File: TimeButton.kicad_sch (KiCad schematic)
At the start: 14 parts, among them P1 USB_C_Plug_USB2.0, U1 PIC18F15Q41-I/SS, U2 FT231XS

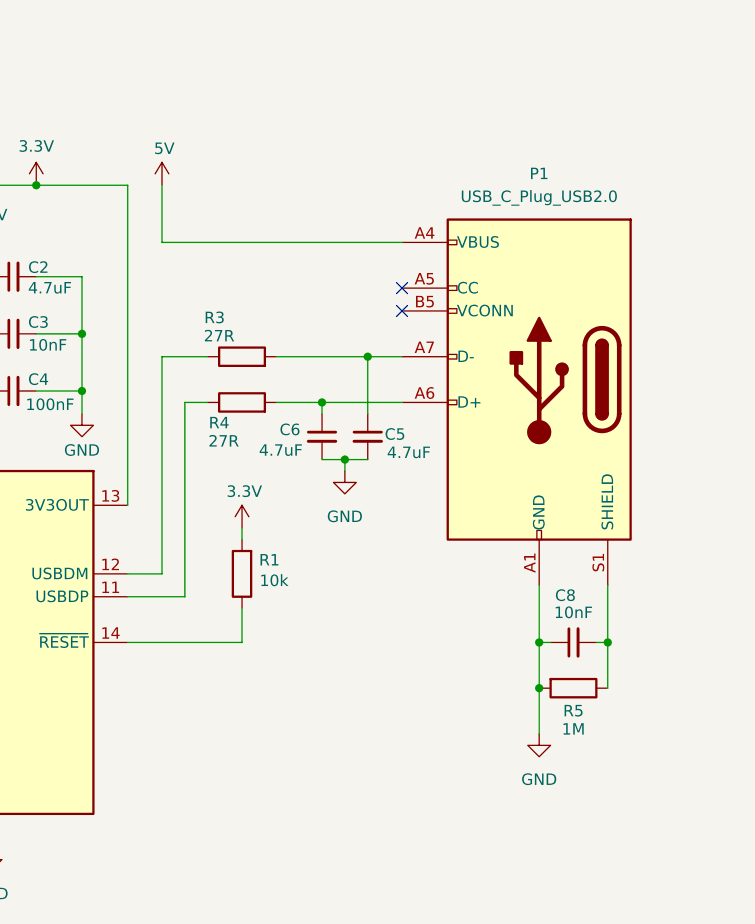
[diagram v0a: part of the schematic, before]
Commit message: Changed USB_C connector from 6Pin to 16Pin
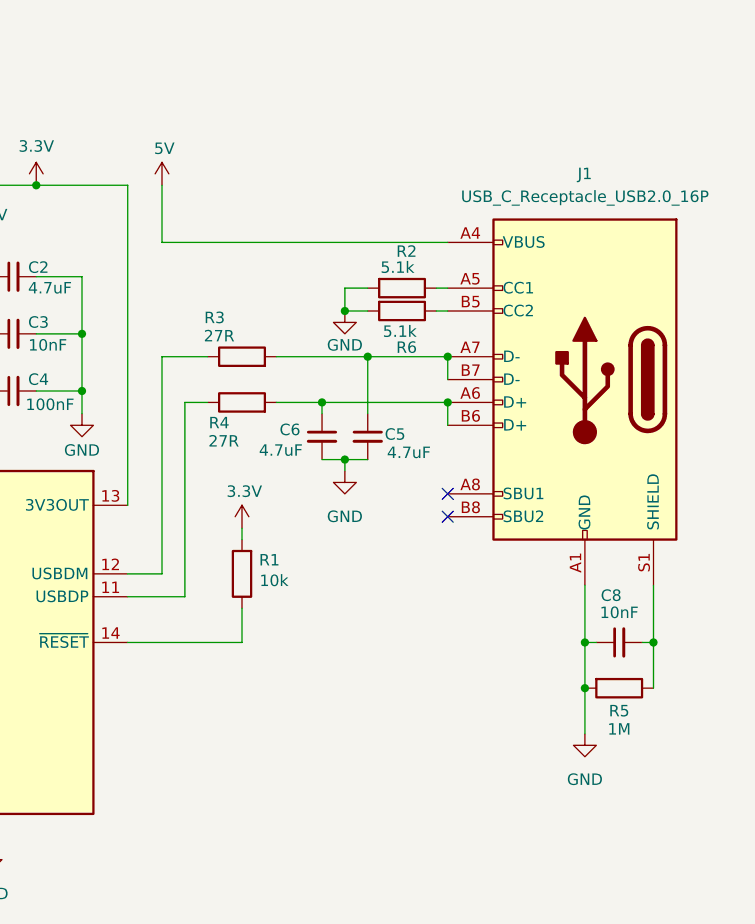
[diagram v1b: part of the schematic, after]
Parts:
- removed P1: USB_C_Plug_USB2.0, Connector_USB:USB_C_Receptacle_HRO_TYPE-C-31-M-17, symbol Connector:USB_C_Plug_USB2.0
- added J1: USB_C_Receptacle_USB2.0_16P, Connector_USB:USB_C_Receptacle_G-Switch_GT-USB-7010ASV, symbol Connector:USB_C_Receptacle_USB2.0_16P
- added R2, R6: 5.1k, symbol Device:R
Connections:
- net 5V: now also J1.A4 (VBUS), J1.A9 (VBUS), J1.B4 (VBUS), J1.B9 (VBUS)
- net GND: now also J1.A1 (GND), J1.A12 (GND), J1.B1 (GND), J1.B12 (GND), R2.2, R6.2
- net at C5.1, R3.2: now also J1.A7 (D-), J1.B7 (D-)
- net at C6.1, R4.2: now also J1.A6 (D+), J1.B6 (D+)
- net at C8.2, R5.1: now also J1.S1 (SHIELD)
- new net: J1.A5 (CC1), R2.1
- new net: J1.B5 (CC2), R6.1
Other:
- moved on the sheet: C8, R5

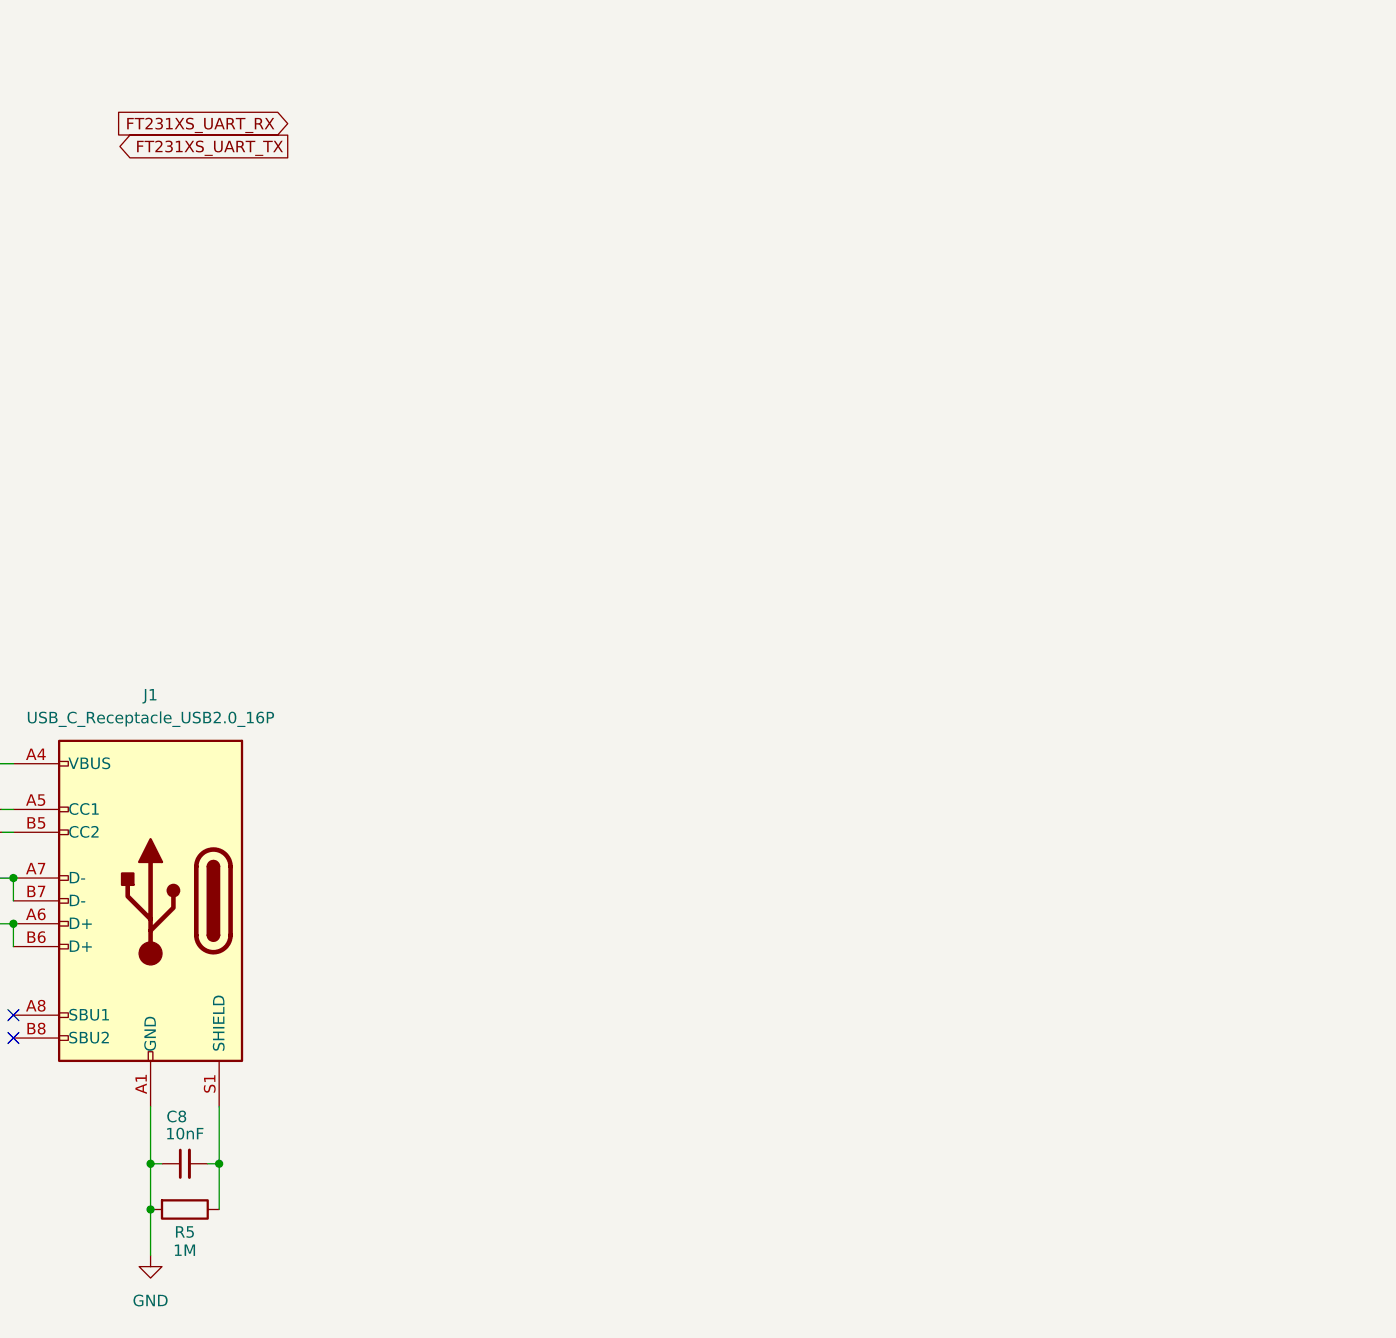
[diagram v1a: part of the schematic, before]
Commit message: Added LEDs
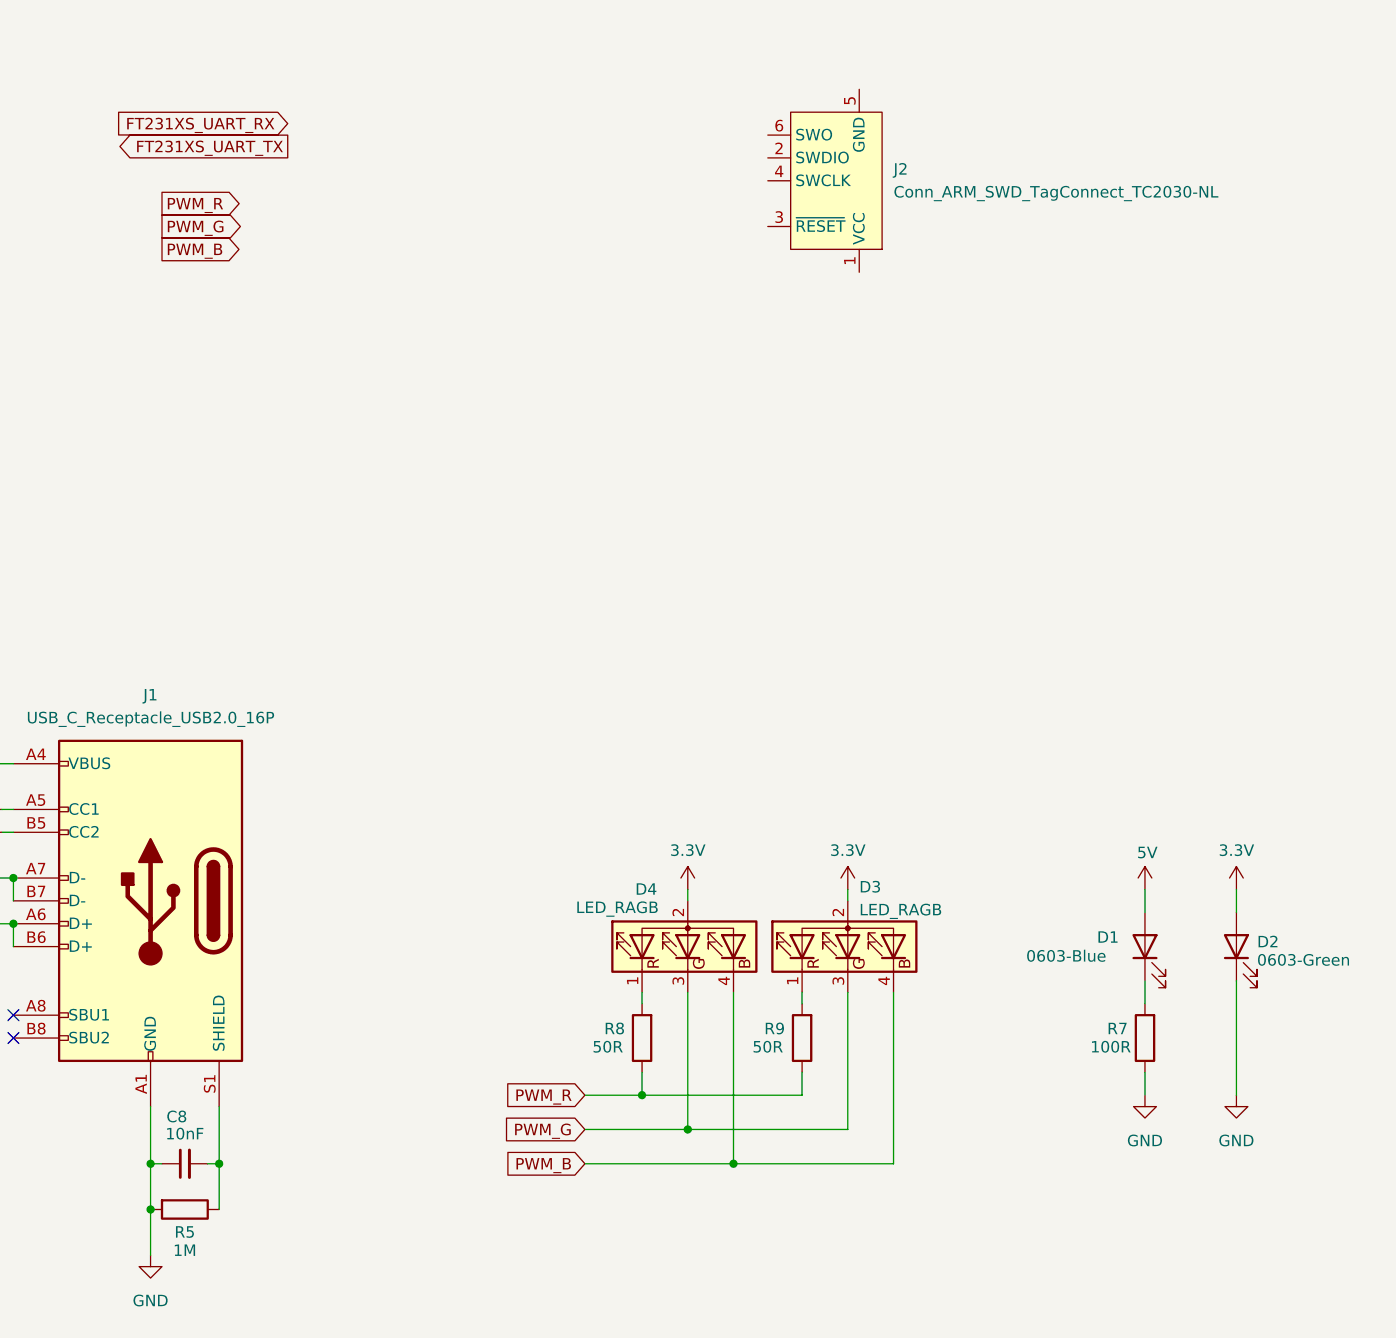
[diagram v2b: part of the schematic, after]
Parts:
- added D1: 0603-Blue, LED_SMD:LED_1206_3216Metric, symbol LED:IR26-21C_L110_TR8
- added D2: 0603-Green, LED_SMD:LED_1206_3216Metric, symbol LED:IR26-21C_L110_TR8
- added D3, D4: LED_RAGB, symbol Device:LED_RAGB
- added J2: Conn_ARM_SWD_TagConnect_TC2030-NL, Connector:Tag-Connect_TC2030-IDC-NL_2x03_P1.27mm_Vertical, symbol Connector:Conn_ARM_SWD_TagConnect_TC2030-NL
- added R7: 100R, symbol Device:R
- added R8, R9: 50R, symbol Device:R
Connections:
- net 3.3V: now also D2.2 (A), D3.2 (A), D4.2 (A)
- net 5V: now also D1.2 (A)
- net GND: now also D2.1 (K), R7.1
- new net: D4.1 (RK), R8.2
- new net: D1.1 (K), R7.2
- new net: D3.1 (RK), R9.2
- new net PWM_B: D3.4 (BK), D4.4 (BK)
- new net PWM_G: D3.3 (GK), D4.3 (GK)
- new net PWM_R: R8.1, R9.1

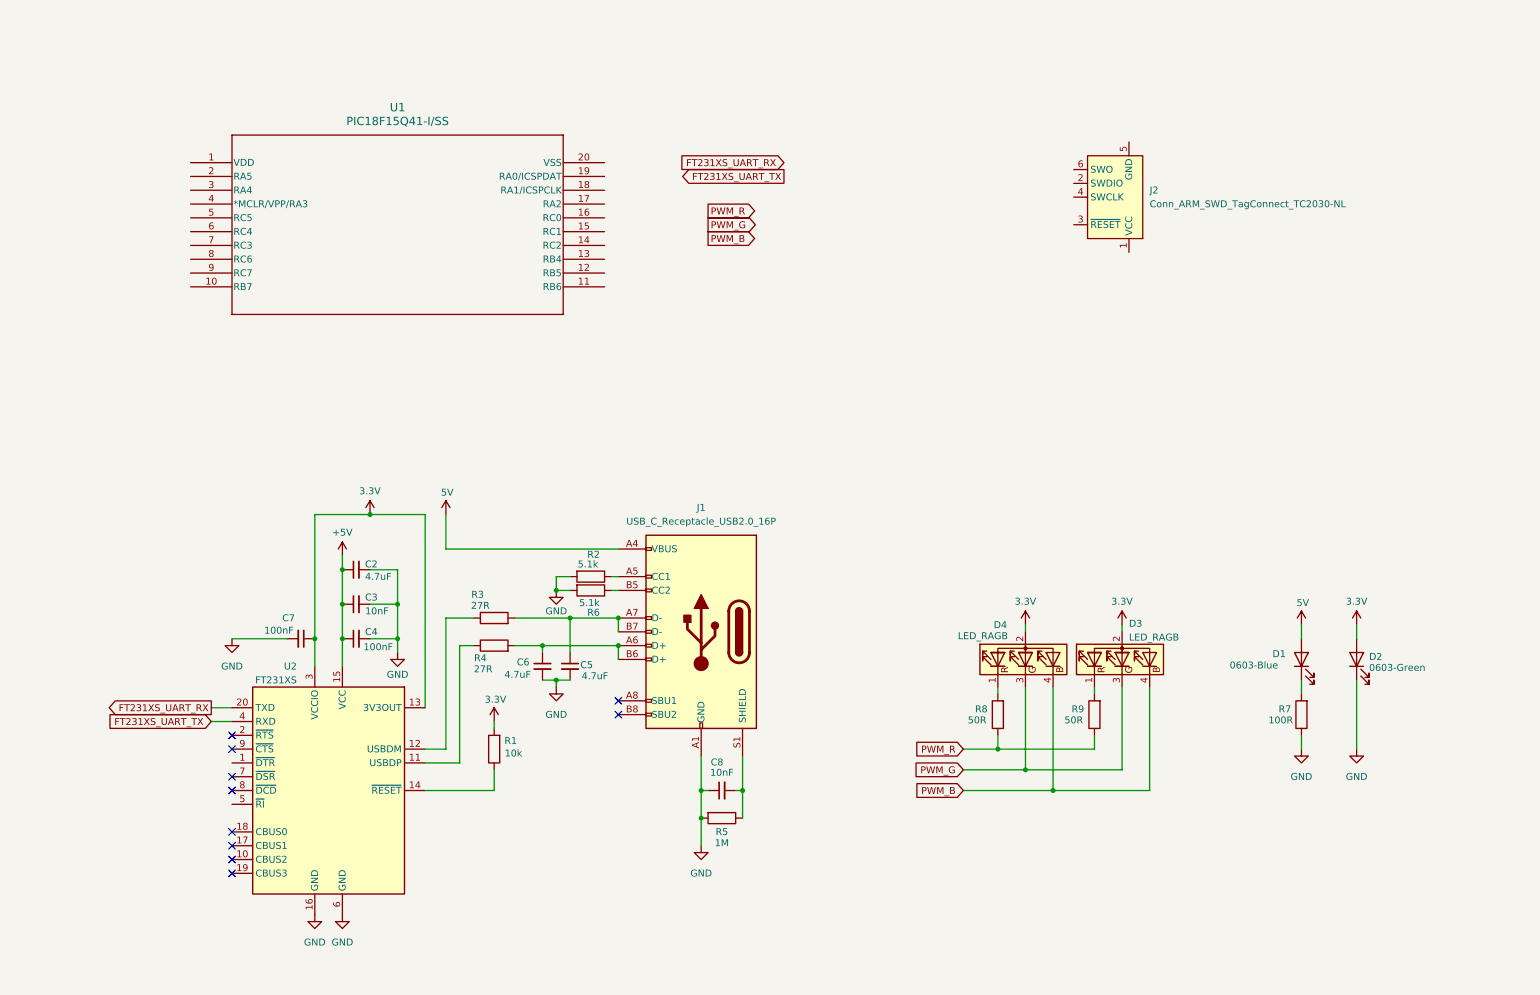
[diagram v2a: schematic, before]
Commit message: Added TagConnect connections in the schematic
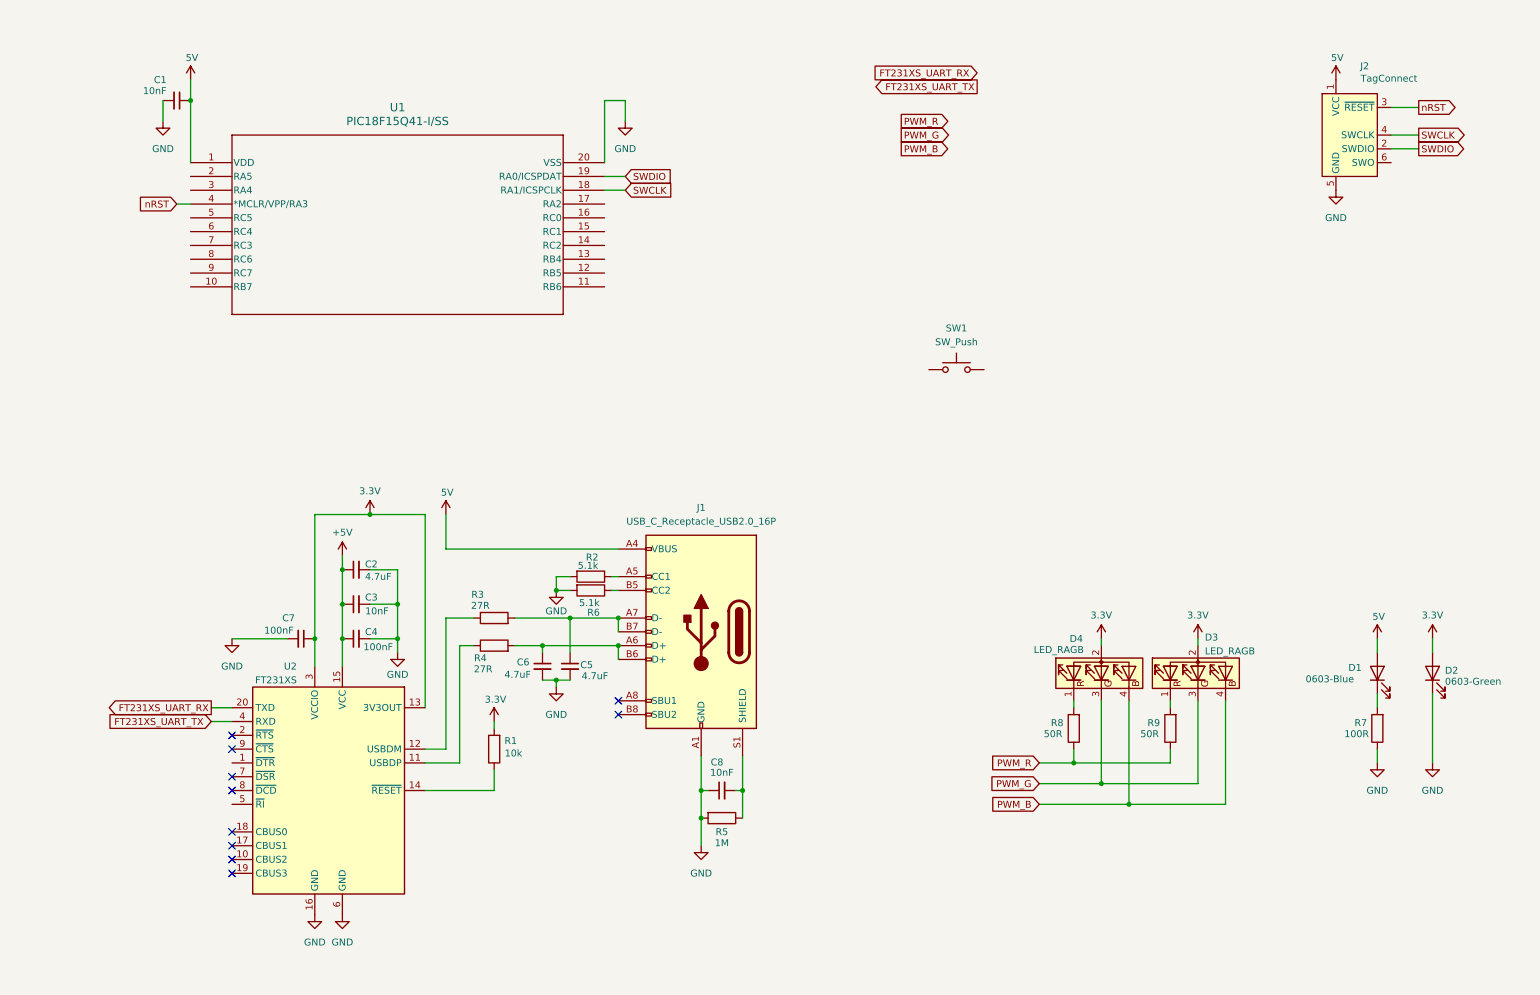
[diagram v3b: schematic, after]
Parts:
- added C1: 10nF, Capacitor_SMD:C_0201_0603Metric_Pad0.64x0.40mm_HandSolder, symbol Device:C_Small
- added SW1: SW_Push, Button_Switch_THT:SW_PUSH-12mm, symbol Switch:SW_Push
- C2, C3, C4, C5, C6, C7, C8: footprint (none) -> Capacitor_SMD:C_0201_0603Metric_Pad0.64x0.40mm_HandSolder
- D3, D4: footprint (none) -> LED_THT:LED_D5.0mm-4_RGB_Wide_Pins
- J2: value Conn_ARM_SWD_TagConnect_TC2030-NL -> TagConnect
- R1, R2, R3, R4, R5, R6, R7, R8, R9: footprint (none) -> Resistor_SMD:R_0201_0603Metric_Pad0.64x0.40mm_HandSolder
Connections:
- net 5V: now also J2.1 (VCC), U1.1 (VDD), C1.1
- net GND: now also J2.5 (GND), U1.20 (VSS), C1.2
- net SWCLK: now reaches U1.18 (RA1/ICSPCLK)
- net SWCLK: now also J2.4 (SWCLK)
- net SWDIO: now reaches U1.19 (RA0/ICSPDAT)
- net SWDIO: now also J2.2 (SWDIO)
- net nRST: now reaches U1.4 (*MCLR/VPP/RA3)
- net nRST: now also J2.3 (~{RESET})
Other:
- moved on the sheet: D1, D2, D3, D4, J2, R7, R8, R9

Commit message: Layout v1.0
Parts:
- removed C1: 10nF, Capacitor_SMD:C_0201_0603Metric_Pad0.64x0.40mm_HandSolder, symbol Device:C_Small
- added J3: Conn_01x05_Pin, Connector_PinHeader_2.00mm:PinHeader_1x05_P2.00mm_Vertical, symbol Connector:Conn_01x05_Pin
- added J4: Conn_01x03_Pin, Connector_PinHeader_2.00mm:PinHeader_1x03_P2.00mm_Vertical, symbol Connector:Conn_01x03_Pin
- C2, C3, C4, C5, C6, C7, C8: footprint Capacitor_SMD:C_0201_0603Metric_Pad0.64x0.40mm_HandSolder -> Capacitor_SMD:C_0805_2012Metric_Pad1.18x1.45mm_HandSolder
- D1, D2: footprint LED_SMD:LED_1206_3216Metric -> LED_SMD:LED_0805_2012Metric_Pad1.15x1.40mm_HandSolder
- R1, R2, R3, R4, R5, R6, R7, R8, R9: footprint Resistor_SMD:R_0201_0603Metric_Pad0.64x0.40mm_HandSolder -> Resistor_SMD:R_0805_2012Metric_Pad1.20x1.40mm_HandSolder
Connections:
- net +5V is gone; now on net 5V: C2.1, C3.1, C4.1, U2.15 (VCC)
- net 3.3V: now also J4.3 (Pin_3)
- net GND: now also SW1.1, J3.1 (Pin_1), J4.1 (Pin_1)
- net PWM_B: now also U1.14 (RC2)
- net PWM_G: now also U1.15 (RC1)
- net PWM_R: now also U1.16 (RC0)
- net at SW1.2: now also U1.17 (RA2)
- net at U1.10 (RB7): now also J3.5 (Pin_5)
- net at U1.12 (RB5): now also J4.2 (Pin_2)
- net at U1.6 (RC4): now also J3.2 (Pin_2)
- net at U1.7 (RC3): now also J3.3 (Pin_3)
- net at U1.9 (RC7): now also J3.4 (Pin_4)
- no-connect marks 10 -> 11
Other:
- moved on the sheet: SW1
